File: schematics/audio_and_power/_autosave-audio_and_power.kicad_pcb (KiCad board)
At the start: 2 copper layers, 85.5 x 101.5 mm, 29 parts, among them J5 Conn_01x03, J6 Conn_01x06, SW1 SW_SPST, SW4 SW_Push, SW5 SW_Push, U2 ESP32-WROOM-32E, U6 MCP4822, U7 PAM8302AAS, U8 LM1117T-3.3

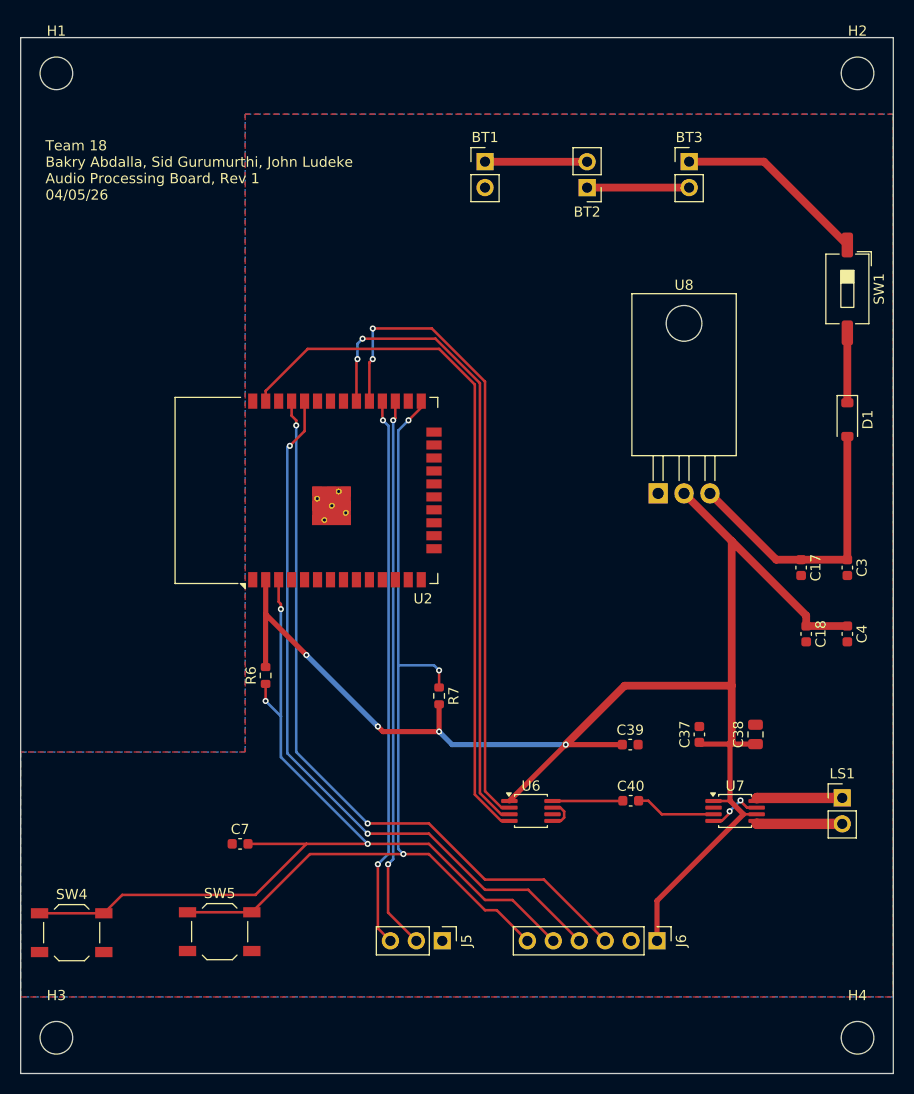
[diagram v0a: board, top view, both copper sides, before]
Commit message: change hole sizes for pcb ordering
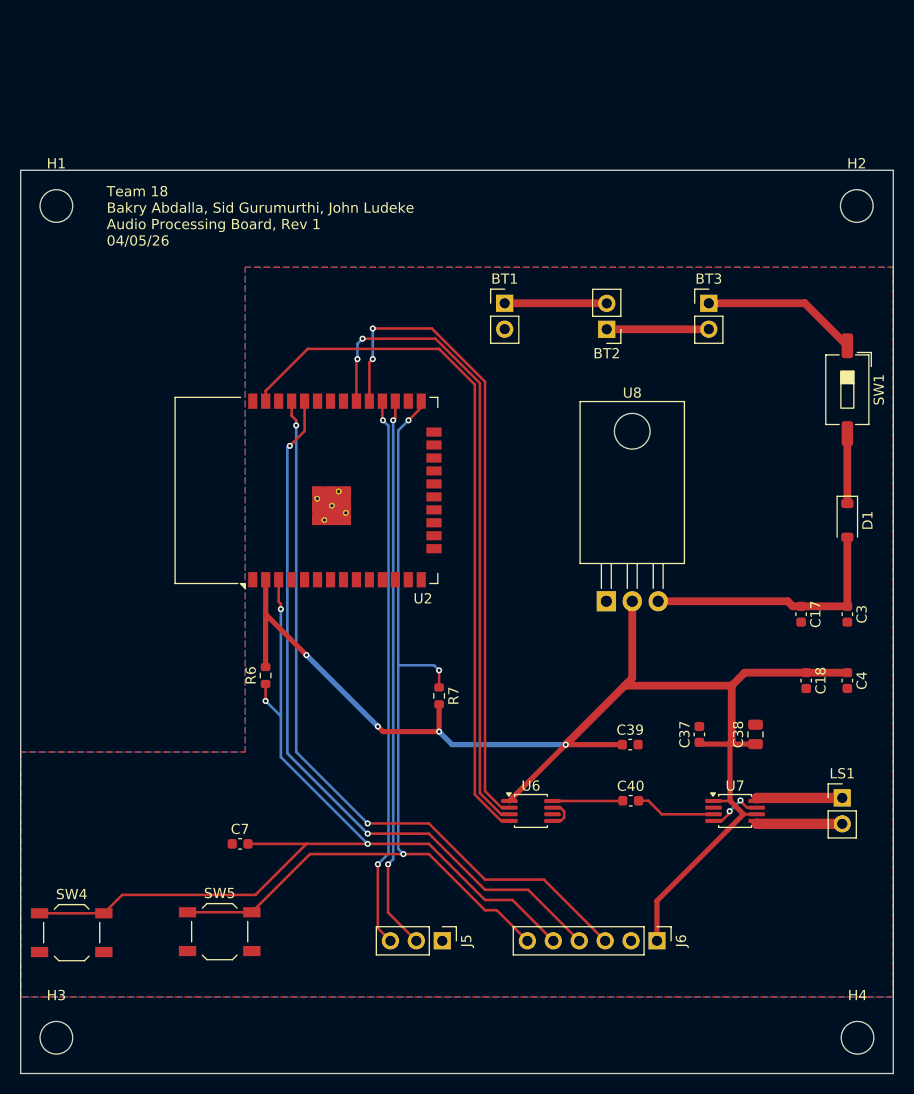
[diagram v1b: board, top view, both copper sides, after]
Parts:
- moved BT1 14.0 mm to (93.5, 76.0)
- moved BT2 14.0 mm to (103.5, 78.6)
- moved BT3 14.0 mm to (113.5, 76.0)
- moved H2 13.0 mm to (128.0, 66.5)
- moved H1 13.0 mm to (49.6, 66.5)
- moved U8 11.7 mm to (103.5, 105.2)
- moved D1 9.88 mm to (127.1, 97.3)
- moved SW1 9.88 mm to (127.1, 84.5)
- moved C17 4.57 mm to (122.5, 106.5)
- moved C18 4.57 mm to (123.0, 113.0)
- moved C3 4.57 mm to (127.1, 106.5)
- moved C4 4.57 mm to (127.1, 113.0)
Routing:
- net /DVDD_3V3: track 151.7 -> 136.0 mm
- net /VBAT: track 18.9 -> 15.3 mm
- net /VBAT_PROT: track 28.2 -> 25.5 mm
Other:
- board size 85.5 x 101.5 mm -> 85.5 x 88.5 mm
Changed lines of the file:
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@@
 	(footprint "Button_Switch_SMD:SW_DIP_SPSTx01_Slide_6.7x4.1mm_W8.61mm_P2.54mm_LowProfile"
 		(layer "F.Cu")
-		(at 127.07375 74.625 -90)
+		(at 127.07375 84.5 -90)
 		(descr "SMD 1x-dip-switch SPST , Slide, row spacing 8.61 mm (338 mils), body size 6.7x4.1mm (see e.g. https://www.ctscorp.com/wp-content/uploads/219.pdf), SMD, LowProfile")
 		(tags "SMD DIP Switch SPST Slide 8.61mm 338mil SMD LowProfile")
@@
 	(footprint "Capacitor_SMD:C_0603_1608Metric"
 		(layer "F.Cu")
-		(at 122.54375 101.93 -90)
+		(at 122.54375 106.5 -90)
 		(descr "Capacitor SMD 0603 (1608 Metric), square (rectangular) end terminal, IPC-7351 nominal, (Body size source: IPC-SM-782 page 76, https://www.pcb-3d.com/wordpress/wp-content/uploads/ipc-sm-782a_amendment_1_and_2.pdf), generated with kicad-footprint-generator")
 		(tags "capacitor")
@@
 	(footprint "Connector_PinHeader_2.54mm:PinHeader_1x02_P2.54mm_Vertical"
 		(layer "F.Cu")
-		(at 111.57375 62.155)
+		(at 113.5 76.03)
 		(descr "Through hole straight pin header, 1x02, 2.54mm pitch, single row")
 		(tags "Through hole pin header THT 1x02 2.54mm single row")
@@
 	(footprint "MountingHole:MountingHole_3.2mm_M3"
 		(layer "F.Cu")
-		(at 49.57375 53.5)
+		(at 49.57375 66.5)
 		(descr "Mounting Hole 3.2mm, M3, no annular, generated by kicad-footprint-generator mountinghole.py")
 		(tags "mountinghole M3")
@@
 	(footprint "Package_TO_SOT_THT:TO-220-3_Horizontal_TabDown"
 		(layer "F.Cu")
-		(at 108.53375 94.66)
+		(at 103.46 105.23)
 		(descr "TO-220-3, Horizontal, RM 2.54mm, see https://www.vishay.com/docs/66542/to-220-1.pdf, generated with kicad-footprint-generator TO_SOT_THT_generate.py")
 		(tags "TO-220-3 Horizontal RM 2.54mm")
@@
 	(footprint "Diode_SMD:D_SOD-123"
 		(layer "F.Cu")
-		(at 127.07375 87.43 -90)
+		(at 127.07375 97.305 -90)
 		(descr "SOD-123")
 		(tags "SOD-123")
@@
 	(footprint "Connector_PinHeader_2.54mm:PinHeader_1x02_P2.54mm_Vertical"
 		(layer "F.Cu")
-		(at 91.57375 62.155)
+		(at 93.5 76.03)
 		(descr "Through hole straight pin header, 1x02, 2.54mm pitch, single row")
 		(tags "Through hole pin header THT 1x02 2.54mm single row")
@@
 	(footprint "MountingHole:MountingHole_3.2mm_M3"
 		(layer "F.Cu")
-		(at 128.07375 53.5)
+		(at 128 66.5)
 		(descr "Mounting Hole 3.2mm, M3, no annular, generated by kicad-footprint-generator mountinghole.py")
 		(tags "mountinghole M3")
@@
 		)
 		(property "Value" "MountingHole"
-			(at 0 4.15 0)
+			(at 0 9.455 0)
 			(layer "F.Fab")
 			(effects
@@
 	(footprint "Capacitor_SMD:C_0603_1608Metric"
 		(layer "F.Cu")
-		(at 127.07375 108.43 -90)
+		(at 127.07375 113 -90)
 		(descr "Capacitor SMD 0603 (1608 Metric), square (rectangular) end terminal, IPC-7351 nominal, (Body size source: IPC-SM-782 page 76, https://www.pcb-3d.com/wordpress/wp-content/uploads/ipc-sm-782a_amendment_1_and_2.pdf), generated with kicad-footprint-generator")
 		(tags "capacitor")
@@
 	(footprint "Connector_PinHeader_2.54mm:PinHeader_1x02_P2.54mm_Vertical"
 		(layer "F.Cu")
-		(at 101.57375 64.705 180)
+		(at 103.5 78.58 180)
 		(descr "Through hole straight pin header, 1x02, 2.54mm pitch, single row")
 		(tags "Through hole pin header THT 1x02 2.54mm single row")
@@
 	(footprint "Capacitor_SMD:C_0603_1608Metric"
 		(layer "F.Cu")
-		(at 123.04375 108.43 -90)
+		(at 123.04375 113 -90)
 		(descr "Capacitor SMD 0603 (1608 Metric), square (rectangular) end terminal, IPC-7351 nominal, (Body size source: IPC-SM-782 page 76, https://www.pcb-3d.com/wordpress/wp-content/uploads/ipc-sm-782a_amendment_1_and_2.pdf), generated with kicad-footprint-generator")
 		(tags "capacitor")
@@
 	(footprint "Capacitor_SMD:C_0603_1608Metric"
 		(layer "F.Cu")
-		(at 127.07375 101.93 -90)
+		(at 127.07375 106.5 -90)
 		(descr "Capacitor SMD 0603 (1608 Metric), square (rectangular) end terminal, IPC-7351 nominal, (Body size source: IPC-SM-782 page 76, https://www.pcb-3d.com/wordpress/wp-content/uploads/ipc-sm-782a_amendment_1_and_2.pdf), generated with kicad-footprint-generator")
 		(tags "capacitor")
@@
 	)
 	(gr_rect
-		(start 46.07375 50)
+		(start 46.07375 63)
 		(end 131.57375 151.5)
 		(stroke
@@
 	)
 	(gr_text "Team 18\nBakry Abdalla, Sid Gurumurthi, John Ludeke\nAudio Processing Board, Rev 1\n04/05/26\n"
-		(at 48.5 66 0)
+		(at 54.5 70.5 0)
 		(layer "F.SilkS")
 		(effects
@@
 		(layer "User.1")
 		(pts
-			(xy 131.57375 50) (xy 46.07375 50)
+			(xy 131.57375 63) (xy 46.07375 63)
 		)
 		(height -10)
@@
 		)
 		(gr_text "85.5"
-			(at 88.82375 38.85 0)
+			(at 88.82375 51.85 0)
 			(layer "User.1")
 			(effects
@@
 		(layer "User.1")
 		(pts
-			(xy 131.57375 151.5) (xy 131.57375 50)
+			(xy 131.57375 151.5) (xy 131.57375 63)
 		)
 		(height 12.5)
@@
 			(keep_text_aligned yes)
 		)
-		(gr_text "101.5"
-			(at 142.92375 100.75 90)
+		(gr_text "88.5"
+			(at 142.92375 107.25 90)
 			(layer "User.1")
 			(effects
@@
 		(layer "User.1")
 		(pts
-			(xy 46.07375 151.5) (xy 46.07375 50)
+			(xy 46.07375 151.5) (xy 46.07375 63)
 		)
 		(height -12)
@@
 			(keep_text_aligned yes)
 		)
-		(gr_text "101.5"
-			(at 32.92375 100.75 90)
+		(gr_text "88.5"
+			(at 32.92375 107.25 90)
 			(layer "User.1")
 			(effects
@@
 	)
 	(segment
-		(start 91.58375 62.165)
-		(end 91.57375 62.155)
+		(start 93.5 76.03)
+		(end 103.49 76.03)
 		(width 0.762)
 		(layer "F.Cu")
@@
 	)
 	(segment
-		(start 101.57375 62.165)
-		(end 91.58375 62.165)
+		(start 103.49 76.03)
+		(end 103.5 76.04)
 		(width 0.762)
 		(layer "F.Cu")
@@
 	)
 	(segment
-		(start 111.57375 64.695)
-		(end 101.58375 64.695)
+		(start 113.49 78.58)
+		(end 113.5 78.57)
 		(width 0.762)
 		(layer "F.Cu")
@@
 	)
 	(segment
-		(start 101.58375 64.695)
-		(end 101.57375 64.705)
+		(start 103.5 78.58)
+		(end 113.49 78.58)
 		(width 0.762)
 		(layer "F.Cu")
@@
 	)
 	(segment
-		(start 111.57375 62.155)
-		(end 118.90875 62.155)
+		(start 122.90875 76.03)
+		(end 127.07375 80.195)
 		(width 0.762)
 		(layer "F.Cu")
@@
 	)
 	(segment
-		(start 118.90875 62.155)
-		(end 127.07375 70.32)
+		(start 113.5 76.03)
+		(end 122.90875 76.03)
 		(width 0.762)
 		(layer "F.Cu")
@@
 	)
 	(segment
-		(start 127.07375 101.155)
-		(end 127.07375 89.08)
+		(start 121.725 105.725)
+		(end 121.23 105.23)
+		(width 0.762)
+		(layer "F.Cu")
+		(net 5)
+	)
+	(segment
+		(start 127.07375 105.725)
+		(end 122.54375 105.725)
 		(width 0.762)
 		(layer "F.Cu")
@@
 	)
 	(segment
-		(start 127.07375 101.155)
-		(end 122.54375 101.155)
+		(start 122.54375 105.725)
+		(end 121.725 105.725)
 		(width 0.762)
 		(layer "F.Cu")
@@
 	)
 	(segment
-		(start 120.10875 101.155)
-		(end 113.61375 94.66)
+		(start 127.07375 98.955)
+		(end 127.07375 105.725)
 		(width 0.762)
 		(layer "F.Cu")
@@
 	)
 	(segment
-		(start 122.54375 101.155)
-		(end 120.10875 101.155)
+		(start 121.23 105.23)
+		(end 108.54 105.23)
 		(width 0.762)
 		(layer "F.Cu")
@@
 	)
 	(segment
+		(start 106 112.75625)
+		(end 105.25625 113.5)
+		(width 0.762)
+		(layer "F.Cu")
+		(net 6)
+	)
+	(segment
 		(start 115.57375 119.225)
 		(end 112.74875 119.225)
@@
 	)
 	(segment
-		(start 115.74375 99.33)
-		(end 111.07375 94.66)
+		(start 106 105.23)
+		(end 106 112.75625)
 		(width 0.762)
 		(layer "F.Cu")
@@
 	)
 	(segment
-		(start 123.04375 106.63)
-		(end 115.74375 99.33)
+		(start 123.04375 112.225)
+		(end 117.01875 112.225)
 		(width 0.762)
 		(layer "F.Cu")
@@
 	)
 	(segment
-		(start 123.04375 107.655)
-		(end 123.04375 106.63)
-		(width 0.762)
-		(layer "F.Cu")
-		(net 6)
-	)
-	(segment
-		(start 127.07375 107.655)
-		(end 123.04375 107.655)
+		(start 127.07375 112.225)
+		(end 123.04375 112.225)
 		(width 0.762)
 		(layer "F.Cu")
@@
 	)
 	(segment
+		(start 117.01875 112.225)
+		(end 115.74375 113.5)
+		(width 0.762)
+		(layer "F.Cu")
+		(net 6)
+	)
+	(segment
 		(start 70.07375 106.52)
 		(end 70.07375 111.675)
@@
 	)
 	(segment
-		(start 115.74375 99.33)
-		(end 115.74375 113.5)
-		(width 0.762)
-		(layer "F.Cu")
-		(net 6)
-	)
-	(segment
 		(start 115.57375 124.775)
 		(end 115.54875 124.8)
@@
 	)
 	(segment
-		(start 127.07375 78.93)
-		(end 127.07375 85.78)
+		(start 127.07375 88.805)
+		(end 127.07375 95.655)
 		(width 0.762)
 		(layer "F.Cu")
@@
 		(polygon
 			(pts
-				(xy 68.07375 57.5) (xy 68.07375 120) (xy 46.07375 120) (xy 46.07375 144) (xy 131.57375 144) (xy 131.57375 57.5)
+				(xy 68.07375 72.5) (xy 68.07375 120) (xy 46.07375 120) (xy 46.07375 144) (xy 131.57375 144) (xy 131.57375 72.5)
 			)
 		)
@@
 		(polygon
 			(pts
-				(xy 68.07375 57.5) (xy 131.57375 57.5) (xy 131.57375 144) (xy 46.07375 144) (xy 46.07375 120) (xy 68.07375 120)
+				(xy 68.07375 72.5) (xy 131.57375 72.5) (xy 131.57375 144) (xy 46.07375 144) (xy 46.07375 120) (xy 68.07375 120)
 			)
 		)
